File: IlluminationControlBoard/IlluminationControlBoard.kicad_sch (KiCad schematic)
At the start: 6 parts, among them J1 LIGHT1OUT, J2 12V_IN, J3 LIGHT2OUT, J4 PWM_SIGNALS

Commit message: SchematicUpdates
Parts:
- J2: footprint (none) -> Connector_Molex:Molex_Mini-Fit_Jr_5566-02A_2x01_P4.20mm_Vertical; symbol Connector_Generic:Conn_01x04 -> Connector_Generic:Conn_01x02
- U1, U2: footprint (none) -> ATMARS_ILLUMINATION:DWE_DRIVER
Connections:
- net 12V: now also J2.2 (Pin_2); no longer J2.3 (Pin_3), J2.4 (Pin_4)
- net GND: no longer J2.2 (Pin_2)
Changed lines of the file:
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@@
 	(generator_version "8.0")
 	(paper "A4")
-	(junction
-		(at 30.48 45.72)
-		(diameter 0)
-		(color 0 0 0 0)
-	)
-	(junction
-		(at 30.48 40.64)
-		(diameter 0)
-		(color 0 0 0 0)
-	)
 	(wire
 		(pts
@@
 	(wire
 		(pts
-			(xy 25.4 40.64) (xy 30.48 40.64)
+			(xy 29.21 40.64) (xy 30.48 40.64)
 		)
 		(stroke
@@
 	(wire
 		(pts
-			(xy 30.48 45.72) (xy 30.48 44.45)
-		)
-		(stroke
-			(width 0)
-			(type default)
-		)
-	)
-	(wire
-		(pts
 			(xy 52.07 81.28) (xy 55.88 81.28)
 		)
@@
 	(wire
 		(pts
-			(xy 30.48 39.37) (xy 33.02 39.37)
-		)
-		(stroke
-			(width 0)
-			(type default)
-		)
-	)
-	(wire
-		(pts
 			(xy 27.94 82.55) (xy 31.75 82.55)
 		)
@@
 	(wire
 		(pts
-			(xy 25.4 45.72) (xy 30.48 45.72)
-		)
-		(stroke
-			(width 0)
-			(type default)
-		)
-	)
-	(wire
-		(pts
-			(xy 30.48 40.64) (xy 30.48 39.37)
-		)
-		(stroke
-			(width 0)
-			(type default)
-		)
-	)
-	(wire
-		(pts
-			(xy 33.02 46.99) (xy 30.48 46.99)
-		)
-		(stroke
-			(width 0)
-			(type default)
-		)
-	)
-	(wire
-		(pts
-			(xy 30.48 44.45) (xy 33.02 44.45)
+			(xy 29.21 44.45) (xy 33.02 44.45)
 		)
 		(stroke
@@
 	(wire
 		(pts
-			(xy 30.48 46.99) (xy 30.48 45.72)
-		)
-		(stroke
-			(width 0)
-			(type default)
-		)
-	)
-	(wire
-		(pts
 			(xy 27.94 29.21) (xy 33.02 29.21)
 		)
@@
 	(global_label "12V"
 		(shape input)
-		(at 25.4 45.72 180)
+		(at 29.21 44.45 180)
 		(fields_autoplaced yes)
 		(effects
@@
 		)
 		(property "Intersheetrefs" "${INTERSHEET_REFS}"
-			(at 18.9072 45.72 0)
+			(at 22.7172 44.45 0)
 			(effects
 				(font
@@
 			)
 		)
-		(property "Footprint" ""
+		(property "Footprint" "ATMARS_ILLUMINATION:DWE_DRIVER"
 			(at 45.72 96.52 0)
 			(effects
@@
 			)
 		)
-		(property "Footprint" ""
+		(property "Footprint" "ATMARS_ILLUMINATION:DWE_DRIVER"
 			(at 45.72 82.55 0)
 			(effects
@@
 	)
 	(symbol
-		(lib_id "Connector_Generic:Conn_01x04")
+		(lib_id "Connector_Generic:Conn_01x02")
 		(at 38.1 41.91 0)
 		(unit 1)
@@
 		(fields_autoplaced yes)
 		(property "Reference" "J2"
-			(at 40.64 41.9099 0)
+			(at 40.132 41.9678 0)
 			(effects
 				(font
@@
 		)
 		(property "Value" "12V_IN"
-			(at 40.64 44.4499 0)
+			(at 40.132 44.3921 0)
 			(effects
 				(font
@@
 			)
 		)
-		(property "Footprint" ""
+		(property "Footprint" "Connector_Molex:Molex_Mini-Fit_Jr_5566-02A_2x01_P4.20mm_Vertical"
 			(at 38.1 41.91 0)
 			(effects
@@
 			)
 		)
-		(property "Description" "Generic connector, single row, 01x04, script generated (kicad-library-utils/schlib/autogen/connector/)"
+		(property "Description" "Generic connector, single row, 01x02, script generated (kicad-library-utils/schlib/autogen/connector/)"
 			(at 38.1 41.91 0)
 			(effects
@@
 			)
 		)
-		(pin "3"
-		)
 		(pin "1"
-		)
-		(pin "4"
 		)
 		(pin "2"
@@
 	(symbol
 		(lib_id "power:GND")
-		(at 25.4 40.64 270)
+		(at 29.21 40.64 270)
 		(unit 1)
 		(exclude_from_sim no)
@@
 		(fields_autoplaced yes)
 		(property "Reference" "#PWR01"
-			(at 19.05 40.64 0)
+			(at 22.86 40.64 0)
 			(effects
 				(font
@@
 		)
 		(property "Value" "GND"
-			(at 21.59 40.6399 90)
+			(at 25.4 40.6399 90)
 			(effects
 				(font
@@
 		)
 		(property "Footprint" ""
-			(at 25.4 40.64 0)
+			(at 29.21 40.64 0)
 			(effects
 				(font
@@
 		)
 		(property "Datasheet" ""
-			(at 25.4 40.64 0)
+			(at 29.21 40.64 0)
 			(effects
 				(font
@@
 		)
 		(property "Description" "Power symbol creates a global label with name \"GND\" , ground"
-			(at 25.4 40.64 0)
-			(effects
-				(font
+			(at 29.21 40.64 0)
+			(effects
+				(font

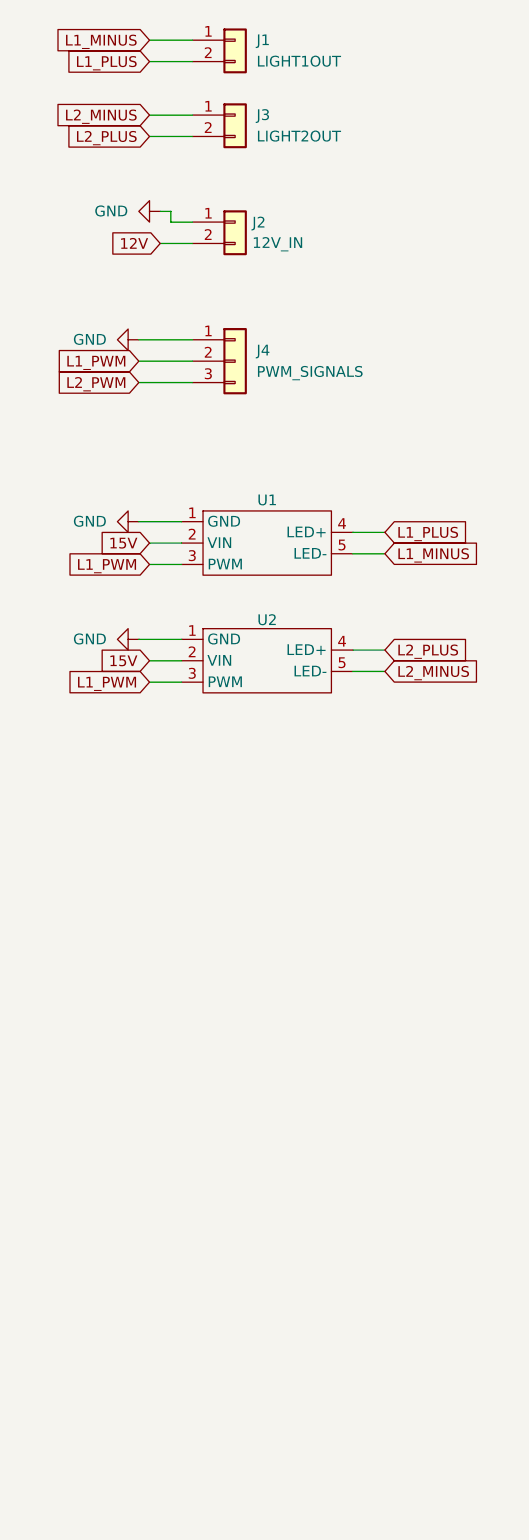
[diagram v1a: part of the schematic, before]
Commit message: PCB designed
Designed and populated PCB to provide 15V to illumination.
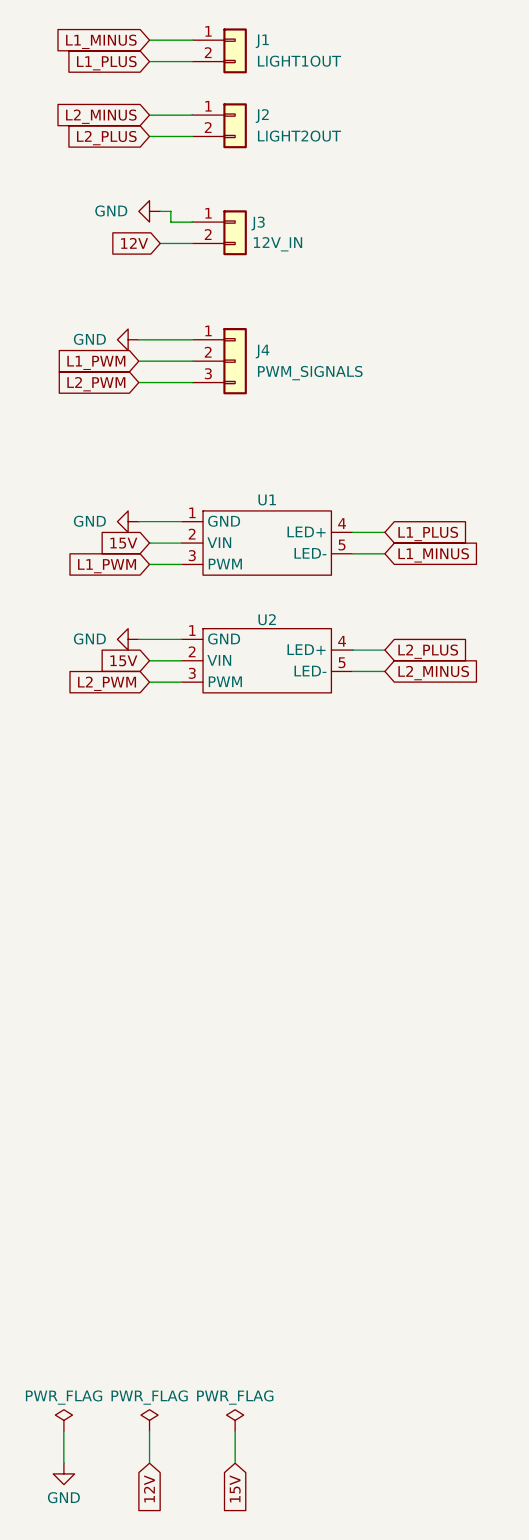
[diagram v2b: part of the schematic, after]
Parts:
- J1: footprint (none) -> Connector_Molex:Molex_SL_171971-0002_1x02_P2.54mm_Vertical; DigikeyPartNumber (none) -> WM4800-ND
- J2: renamed from J3; footprint (none) -> Connector_Molex:Molex_SL_171971-0002_1x02_P2.54mm_Vertical; DigikeyPartNumber (none) -> WM4800-ND
- J4: footprint (none) -> Connector_Molex:Molex_SL_171971-0003_1x03_P2.54mm_Vertical; DigikeyPartNumber (none) -> WM4825-ND
- renumbered J2 to J3
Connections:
- net L1_PWM: no longer U2.3 (PWM)
- net L2_PWM: now also U2.3 (PWM)
